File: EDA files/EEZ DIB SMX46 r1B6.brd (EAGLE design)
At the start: 146 x 95 mm, 144 parts, among them IC1 STM32F030C6T6, IC2 74HC1G126GW,125, IC3 M24C32-WMN6P, IC4 LP2985-33DBVR, IC5 74HC2G04GW,125, IC6 OPA2990IDR, K1 FTR-C1GA012G-B05, K10 FTR-C1GA012G-B05, K11 FTR-C1GA012G-B05, K12 FTR-C1GA012G-B05, K13 FTR-C1GA012G-B05, K14 FTR-C1GA012G-B05, K15 FTR-C1GA012G-B05, K16 FTR-C1GA012G-B05, K17 FTR-C1GA012G-B05, K18 FTR-C1GA012G-B05, K19 RT424005, K2 FTR-C1GA012G-B05, K20 FTR-C1GA012G-B05, K21 FTR-C1GA012G-B05, K22 FTR-C1GA012G-B05, K23 FTR-C1GA012G-B05, K24 FTR-C1GA012G-B05, K25 FTR-C1GA012G-B05, K3 FTR-C1GA012G-B05, K4 FTR-C1GA012G-B05, K5 FTR-C1GA012G-B05, K6 FTR-C1GA012G-B05, K7 FTR-C1GA012G-B05, K8 FTR-C1GA012G-B05, K9 FTR-C1GA012G-B05, Q1 2N7002, Q10 2N7002, Q11 2N7002, Q12 2N7002, Q13 2N7002, Q14 2N7002, Q15 2N7002, Q16 2N7002, Q17 2N7002, Q18 2N7002, Q19 2N7002, Q2 2N7002, Q20 2N7002, Q21 2N7002, Q22 2N7002, Q23 2N7002, Q24 2N7002, Q25 2N7002, Q3 2N7002, Q4 2N7002, Q5 2N7002, Q6 2N7002, Q7 2N7002, Q8 2N7002, Q9 2N7002, X1 N.C., X2 77317-104-28LF, X3 691327310016, X4 691327310016, X6 DS1014-10RF1B, X7 DS1014-10RF1B

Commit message: ADIB ID=001
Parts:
- moved Q2 1.40 mm to (32.3, 85.2)
- moved Q3 1.40 mm to (28.4, 85.2)
- moved Q10 0.63 mm to (77.5, 85.2)
- moved Q11 0.63 mm to (73.7, 85.2)
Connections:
- new net N$10: X6.10, X6.7
- new net N$11: X7.10, X7.7
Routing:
- net N$11: track 0.00 -> 2.83 mm
- net N$10: track 0.00 -> 2.83 mm
- net OUT0: track 219.0 -> 221.7 mm
- net N$39: track 21.3 -> 22.7 mm
- net N$43: track 6.92 -> 8.32 mm
- net OUT1: track 224.3 -> 225.3 mm
- net GND: track 133.9 -> 132.9 mm
- net OUT8: track 182.0 -> 181.4 mm
- net Y3B: track 156.8 -> 156.2 mm
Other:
- board text added: "EEZ DIB SMX46 (12/2020 r1B6)"
- board text added: "EEZ DIB SMX46 (12/2020 r1B6) Project source code: github.com/eez-open"
- board text removed: "EEZ DIB SMX46 (12/2020 r1B5)"
- board text removed: "EEZ DIB SMX46 (12/2020 r1B5) Project source code: github.com/eez-open"

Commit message: RN2 value update
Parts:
- RN2: value DR1206-10K-4/8 -> DR1206-47K-4/8
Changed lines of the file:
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@@
 <attribute name="VALUE" x="84.074" y="18.669" size="1.016" layer="27" ratio="10" rot="R270"/>
 </element>
-<element name="RN2" library="EEZ_Lib1" package="CAY16" value="DR1206-10K-4/8" x="103.8225" y="11.811" smashed="yes" rot="R270">
+<element name="RN2" library="EEZ_Lib1" package="CAY16" value="DR1206-47K-4/8" x="103.8225" y="11.811" smashed="yes" rot="R270">
 <attribute name="NAME" x="102.489" y="13.7795" size="1.016" layer="25" ratio="10"/>
 <attribute name="VALUE" x="103.8225" y="11.811" size="0.8128" layer="27" ratio="10" rot="R270" align="center"/>

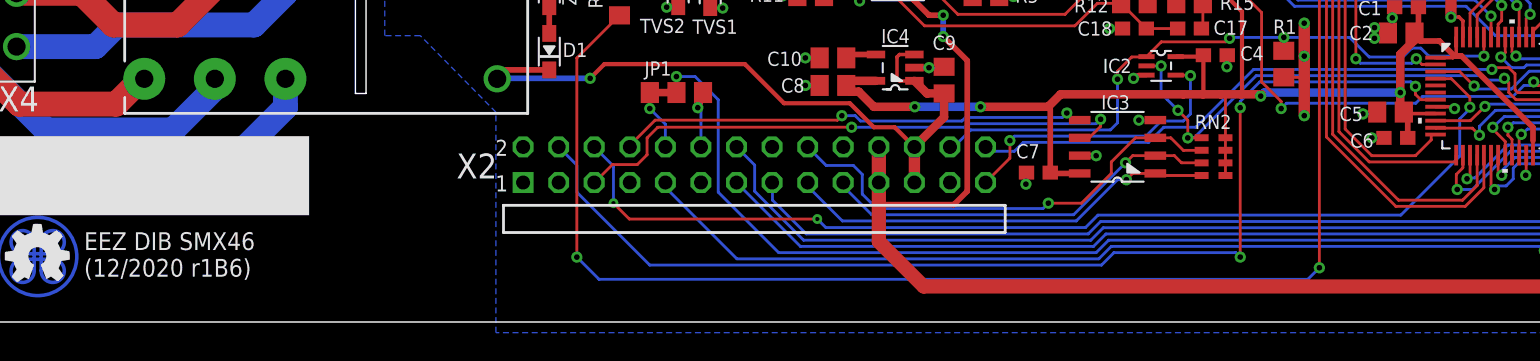
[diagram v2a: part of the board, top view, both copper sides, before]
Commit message: PCB ID added
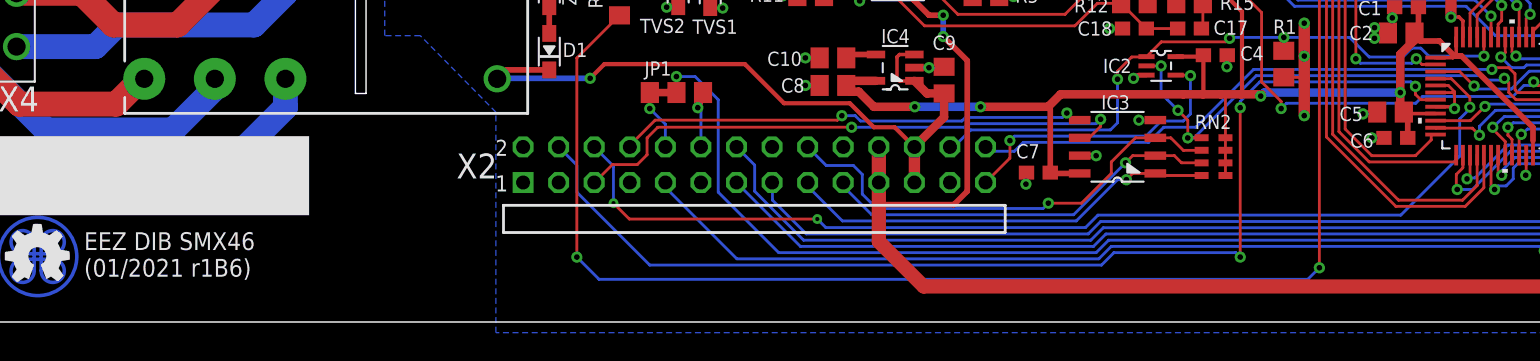
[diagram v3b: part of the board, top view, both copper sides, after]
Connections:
- net GND: now also IC1.5, IC1.6
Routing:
- net GND: track 132.9 -> 137.1 mm
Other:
- board text added: "EEZ DIB SMX46 (01/2021 r1B6)"
- board text added: "EEZ DIB SMX46 (01/2021 r1B6) Project source code: github.com/eez-open"
- board text removed: "EEZ DIB SMX46 (12/2020 r1B6)"
- board text removed: "EEZ DIB SMX46 (12/2020 r1B6) Project source code: github.com/eez-open"
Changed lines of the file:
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@@
 <layer number="56" name="wert" color="7" fill="1" visible="no" active="no"/>
 <layer number="57" name="tCAD" color="7" fill="1" visible="no" active="no"/>
+<layer number="88" name="SimResults" color="9" fill="1" visible="yes" active="yes"/>
+<layer number="89" name="SimProbes" color="9" fill="1" visible="yes" active="yes"/>
 <layer number="90" name="Modules" color="7" fill="1" visible="no" active="no"/>
 <layer number="91" name="Nets" color="2" fill="1" visible="no" active="no"/>
@@
 <layer number="113" name="bTPoint" color="7" fill="1" visible="no" active="no"/>
 <layer number="114" name="Änderung" color="7" fill="1" visible="no" active="no"/>
+<layer number="115" name="CH1" color="13" fill="1" visible="yes" active="yes"/>
 <layer number="116" name="Patch_BOT" color="7" fill="1" visible="no" active="no"/>
+<layer number="117" name="CH2" color="9" fill="1" visible="yes" active="yes"/>
 <layer number="118" name="Rect_Pads" color="7" fill="1" visible="no" active="no"/>
+<layer number="119" name="CH3" color="12" fill="1" visible="yes" active="yes"/>
 <layer number="120" name="lotbs" color="7" fill="1" visible="no" active="no"/>
 <layer number="121" name="_tsilk" color="7" fill="1" visible="no" active="no"/>
@@
 <layer number="127" name="_tValues" color="7" fill="1" visible="no" active="no"/>
 <layer number="128" name="_bValues" color="7" fill="1" visible="no" active="no"/>
+<layer number="129" name="sram_cmd" color="13" fill="1" visible="yes" active="yes"/>
+<layer number="130" name="sram_ctrl" color="2" fill="1" visible="yes" active="yes"/>
 <layer number="131" name="tAdjust" color="7" fill="1" visible="no" active="no"/>
 <layer number="132" name="bAdjust" color="7" fill="1" visible="no" active="no"/>
@@
 <dimension x1="-10" y1="81" x2="-11" y2="17" x3="-12" y3="49" textsize="2" layer="47" dtype="vertical"/>
 <text x="23.1675" y="3.2345" size="1.27" layer="21" font="vector" ratio="10" rot="SR0">EEZ DIB SMX46
-(12/2020 r1B6)</text>
-<text x="143.8234" y="83.4223" size="1.27" layer="22" font="vector" ratio="10" rot="SMR0">EEZ DIB SMX46 (12/2020 r1B6)
+(01/2021 r1B6)</text>
+<text x="143.8234" y="83.4223" size="1.27" layer="22" font="vector" ratio="10" rot="SMR0">EEZ DIB SMX46 (01/2021 r1B6)
 Project source code: github.com/eez-open</text>
 <rectangle x1="17.145" y1="7.62" x2="39.243" y2="13.2715" layer="21"/>
@@
 <wire x1="47.5615" y1="81.319" x2="47.8545" y2="81.319" width="0.2032" layer="1"/>
 <wire x1="47.8545" y1="81.319" x2="48.641" y2="82.1055" width="0.2032" layer="1"/>
+<contactref element="IC1" pad="6"/>
+<contactref element="IC1" pad="5"/>
+<wire x1="119.6721" y1="16.891" x2="120.5865" y2="16.891" width="0.2032" layer="1"/>
+<wire x1="120.5865" y1="16.891" x2="121.031" y2="16.4465" width="0.2032" layer="1"/>
+<wire x1="121.031" y1="16.4465" x2="121.031" y2="16.256" width="0.2032" layer="1"/>
+<wire x1="121.031" y1="16.256" x2="121.031" y2="15.24" width="0.2032" layer="1"/>
+<wire x1="119.6721" y1="16.383" x2="120.904" y2="16.383" width="0.2032" layer="1"/>
+<wire x1="120.904" y1="16.383" x2="121.031" y2="16.256" width="0.2032" layer="1"/>
 </signal>
 <signal name="N$21">
